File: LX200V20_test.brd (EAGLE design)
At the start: 74.9 x 45.7 mm, 32 parts

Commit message: Updated layout.
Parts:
- added STANDOFF5: STAND-OFF, SparkFun-Electromechanical:STAND-OFF
- added U$9: VREG-OKI-78SR, BlueRobotics-Main:OKI-78SR
- moved LED3 54.3 mm to (3.17, 32.4), turned to 270 degrees
- moved R7 54.3 mm to (3.17, 35.6), turned to 180 degrees
- moved LED4 53.5 mm to (3.17, 25.4), turned to 270 degrees
- moved R8 53.5 mm to (3.17, 28.6), turned to 180 degrees
- moved U$1 46.7 mm to (8.89, 3.81), turned to 90 degrees
- moved LED2 46.2 mm to (3.17, 17.8), turned to 270 degrees
- moved R6 46.2 mm to (3.17, 21.0), turned to 180 degrees
- moved LED1 42.2 mm to (3.17, 10.2), turned to 270 degrees
- moved R5 42.2 mm to (3.17, 13.3), turned to 180 degrees
- moved U$2 39.2 mm to (38.1, 18.4), turned to 0 degrees
- moved C4 34.4 mm to (20.3, 7.62), turned to 180 degrees
- moved U$3 29.6 mm to (16.5, 13.3), turned to 0 degrees
- moved C6 22.2 mm to (17.1, 19.7), turned to 180 degrees
- moved U$4 21.5 mm to (14.6, 38.1), turned to 270 degrees
- moved C1 21.0 mm to (17.1, 41.3), turned to 180 degrees
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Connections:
- removed net LED2: U$1.12
- net LED-ACT: now also U$1.12

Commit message: Removed AC components for DC-only support.
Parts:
- removed C5: 0.01uF 250V, resistor:C0805
- removed R9: 4.7K 1/4W, resistor:R1206
- C6: value 0.01uF 250V -> 0.01uF 500V; device resistor:C0805 -> resistor:C1206
- R10: value 4.7K 1/4W -> 10 1/4W
- moved C4 6.99 mm to (20.3, 14.6)
- moved U$3 5.12 mm to (14.0, 8.89)
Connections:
- removed net AC_CPLD_N: R9.2, U$3.6, U$5.2
- removed net N$12: C5.1, R9.1
- net EXT_AC_A: no longer C5.2
- net GND: now also U$3.6, U$5.2
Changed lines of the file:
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@@
 <element name="C2" library="resistor" package="C0402" value="0.1uF" x="17.145" y="26.035"/>
 <element name="C3" library="resistor" package="C1206" value="EFI Capacitor (1000 pF, 2kV)" x="29.845" y="33.655"/>
-<element name="C4" library="resistor" package="C0805" value="330pF 50V" x="20.32" y="7.62" rot="R180"/>
-<element name="C5" library="resistor" package="C0805" value="0.01uF 250V" x="17.145" y="22.225" rot="R180"/>
-<element name="C6" library="resistor" package="C0805" value="0.01uF 250V" x="17.145" y="19.685" rot="R180"/>
+<element name="C4" library="resistor" package="C0805" value="330pF 50V" x="20.32" y="14.605" rot="R180"/>
+<element name="C6" library="resistor" package="C1206" value="0.01uF 500V" x="17.145" y="19.685" rot="R180"/>
 <element name="LED1" library="led" package="CHIPLED_0603" value="" x="3.175" y="10.16" rot="R270"/>
 <element name="LED2" library="led" package="CHIPLED_0603" value="" x="3.175" y="17.78" rot="R270"/>
@@
 <element name="LED4" library="led" package="CHIPLED_0603" value="" x="3.175" y="25.4" rot="R270"/>
 <element name="R1" library="resistor" package="R0603" value="75" x="26.67" y="30.48" rot="R180"/>
-<element name="R10" library="resistor" package="R1206" value="4.7K 1/4W" x="22.225" y="19.685"/>
+<element name="R10" library="resistor" package="R1206" value="10 1/4W" x="22.225" y="19.685"/>
 <element name="R2" library="resistor" package="R0603" value="75" x="26.67" y="36.83" rot="R180"/>
 <element name="R3" library="resistor" package="R0603" value="75" x="30.48" y="36.83"/>
@@
 <element name="R7" library="resistor" package="R0603" value="470" x="3.175" y="35.56" rot="R180"/>
 <element name="R8" library="resistor" package="R0603" value="130" x="3.175" y="28.575" rot="R180"/>
-<element name="R9" library="resistor" package="R1206" value="4.7K 1/4W" x="22.225" y="22.225"/>
 <element name="U$1" library="BR-Eagle-Library" package="LX200V20" value="LX200V20" x="8.89" y="3.81" rot="R90"/>
 <element name="U$2" library="SparkFun-Connectors" package="RJ45-8" value="RJ45-8PTH" x="38.1" y="18.415"/>
-<element name="U$3" library="BlueRobotics-Main" package="PLC10005345" value="PLC10005345" x="16.51" y="13.335"/>
+<element name="U$3" library="BlueRobotics-Main" package="PLC10005345" value="PLC10005345" x="13.97" y="8.89"/>
 <element name="U$4" library="BlueRobotics-Main" package="PT61017PL" value="PT61017PEL" x="14.605" y="38.1" rot="R270"/>
 <element name="U$5" library="BlueRobotics-Main" package="SOD323-BIDIRECTIONAL" value="TVS-SP4021" x="26.035" y="20.955" rot="R90"/>
@@
 <contactref element="LED3" pad="C"/>
 <contactref element="LED4" pad="C"/>
-<wire x1="17.795" y1="26.035" x2="31.245" y2="33.655" width="0" layer="19" extent="1-1"/>
+<contactref element="U$5" pad="2"/>
+<contactref element="U$3" pad="6"/>
+<wire x1="26.035" y1="22.055" x2="31.245" y2="33.655" width="0" layer="19" extent="1-1"/>
+<wire x1="17.795" y1="26.035" x2="26.035" y2="22.055" width="0" layer="19" extent="1-1"/>
 <wire x1="7.49" y1="23.81" x2="17.795" y2="26.035" width="0" layer="19" extent="1-1"/>
 <wire x1="3.925" y1="25.4" x2="7.49" y2="23.81" width="0" layer="19" extent="1-1"/>
@@
 <wire x1="7.49" y1="3.81" x2="10.29" y2="9.81" width="0" layer="19" extent="1-1"/>
 <wire x1="16.495" y1="41.275" x2="7.49" y2="35.81" width="0" layer="19" extent="1-1"/>
+<wire x1="24.13" y1="6.35" x2="10.29" y2="9.81" width="0" layer="19" extent="1-1"/>
 </signal>
 <signal name="N$1">
@@
 <contactref element="U$3" pad="2"/>
 <contactref element="C4" pad="1"/>
-<wire x1="21.27" y1="7.62" x2="19.05" y2="10.795" width="0" layer="19" extent="1-1"/>
-<wire x1="10.29" y1="5.81" x2="19.05" y2="10.795" width="0" layer="19" extent="1-1"/>
+<wire x1="16.51" y1="6.35" x2="21.27" y2="14.605" width="0" layer="19" extent="1-1"/>
+<wire x1="10.29" y1="5.81" x2="16.51" y2="6.35" width="0" layer="19" extent="1-1"/>
 </signal>
 <signal name="TX-">
@@
 <contactref element="U$3" pad="1"/>
 <contactref element="C4" pad="2"/>
-<wire x1="19.37" y1="7.62" x2="19.05" y2="15.875" width="0" layer="19" extent="1-1"/>
-<wire x1="7.49" y1="7.81" x2="19.37" y2="7.62" width="0" layer="19" extent="1-1"/>
+<wire x1="16.51" y1="11.43" x2="19.37" y2="14.605" width="0" layer="19" extent="1-1"/>
+<wire x1="7.49" y1="7.81" x2="16.51" y2="11.43" width="0" layer="19" extent="1-1"/>
 </signal>
 <signal name="RX+">
 <contactref element="U$1" pad="5"/>
 <contactref element="U$3" pad="3"/>
-<wire x1="7.49" y1="11.81" x2="16.51" y2="15.875" width="0" layer="19" extent="1-1"/>
+<wire x1="7.49" y1="11.81" x2="13.97" y2="11.43" width="0" layer="19" extent="1-1"/>
 </signal>
 <signal name="RX-">
 <contactref element="U$1" pad="6"/>
 <contactref element="U$3" pad="4"/>
-<wire x1="10.29" y1="13.81" x2="16.51" y2="10.795" width="0" layer="19" extent="1-1"/>
+<wire x1="13.97" y1="6.35" x2="10.29" y2="13.81" width="0" layer="19" extent="1-1"/>
 </signal>
 <signal name="ZC_IN_EX">
 <contactref element="U$1" pad="8"/>
-</signal>
-<signal name="AC_CPLD_N">
-<contactref element="U$3" pad="6"/>
-<contactref element="R9" pad="2"/>
-<contactref element="U$5" pad="2"/>
-<wire x1="23.647" y1="22.225" x2="26.035" y2="22.055" width="0" layer="19" extent="1-1"/>
-<wire x1="26.67" y1="10.795" x2="26.035" y2="22.055" width="0" layer="19" extent="1-1"/>
 </signal>
 <signal name="N$6">
@@
 <contactref element="R10" pad="1"/>
 <contactref element="C6" pad="1"/>
-<wire x1="18.095" y1="19.685" x2="20.803" y2="19.685" width="0" layer="19" extent="1-1"/>
-</signal>
-<signal name="N$12">
-<contactref element="R9" pad="1"/>
-<contactref element="C5" pad="1"/>
-<wire x1="18.095" y1="22.225" x2="20.803" y2="22.225" width="0" layer="19" extent="1-1"/>
+<wire x1="18.545" y1="19.685" x2="20.803" y2="19.685" width="0" layer="19" extent="1-1"/>
 </signal>
 <signal name="EXT_AC_A">
-<contactref element="C5" pad="2"/>
 <contactref element="JP1" pad="3"/>
-<wire x1="16.195" y1="22.225" x2="36.845" y2="6.35" width="0" layer="19" extent="1-1"/>
 </signal>
 <signal name="EXT_AC_B">
 <contactref element="C6" pad="2"/>
 <contactref element="JP1" pad="4"/>
-<wire x1="16.195" y1="19.685" x2="40.345" y2="6.35" width="0" layer="19" extent="1-1"/>
+<wire x1="15.745" y1="19.685" x2="40.345" y2="6.35" width="0" layer="19" extent="1-1"/>
 </signal>
 <signal name="AC_CPLD_L">
@@
 <contactref element="U$5" pad="1"/>
 <wire x1="23.647" y1="19.685" x2="26.035" y2="19.855" width="0" layer="19" extent="1-1"/>
-<wire x1="26.67" y1="15.875" x2="26.035" y2="19.855" width="0" layer="19" extent="1-1"/>
+<wire x1="24.13" y1="11.43" x2="23.647" y2="19.685" width="0" layer="19" extent="1-1"/>
 </signal>
 </signals>

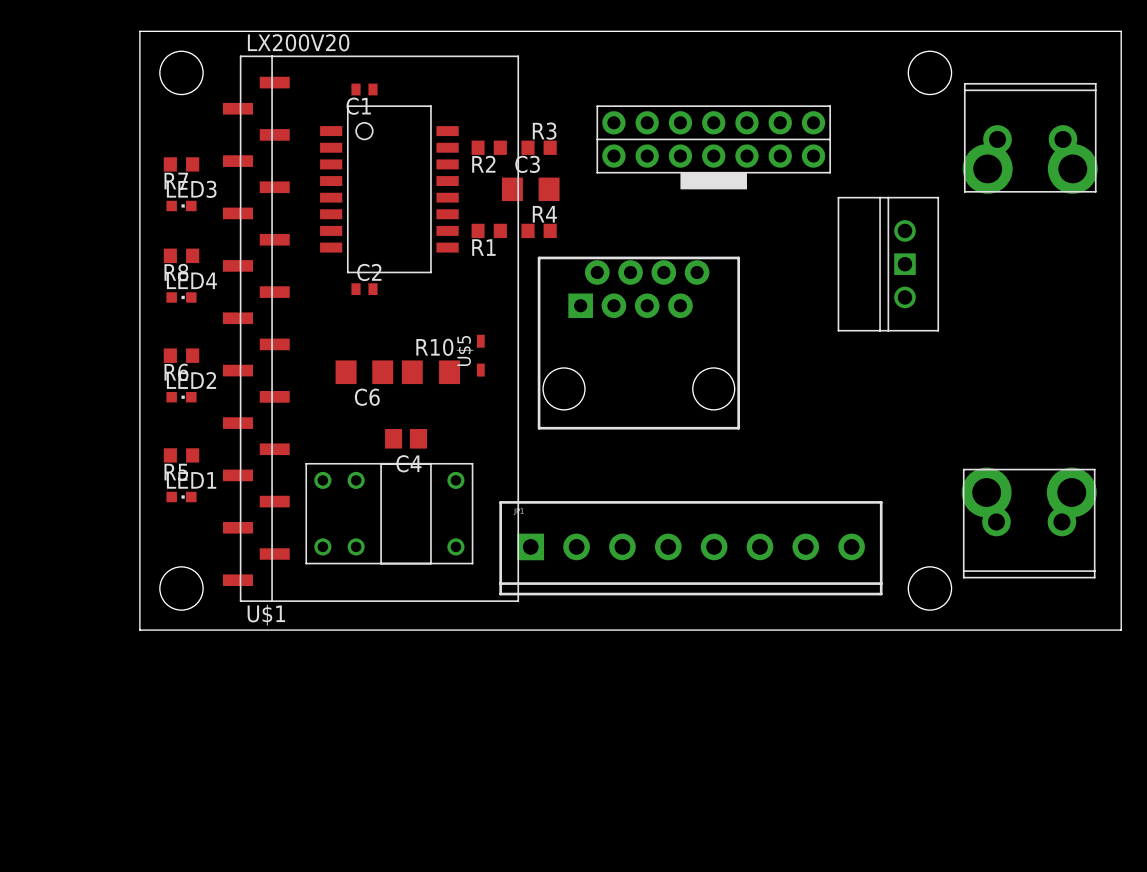
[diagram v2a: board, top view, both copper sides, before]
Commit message: Changing to Ethernet+Power only design.
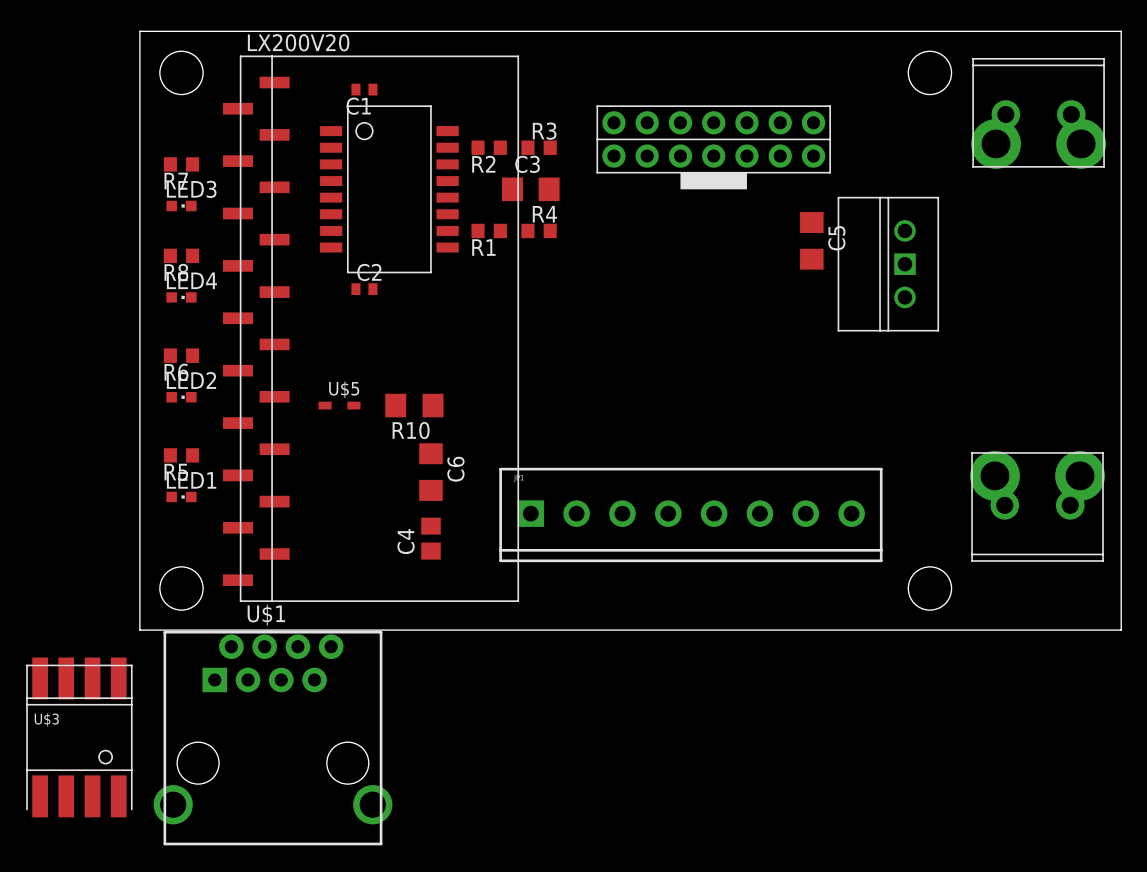
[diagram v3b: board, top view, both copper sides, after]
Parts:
- added C5: 10uF, resistor:C1206
- R10: value 10 1/4W -> 10 1/4W HV
- U$2: device SparkFun-Connectors:RJ45-8 -> BlueRobotics-Main:RJ45-8-VERT
- U$3: value PLC10005345 -> UT11403S; device BlueRobotics-Main:PLC10005345 -> BlueRobotics-Main:UT11403S
- U$9: value VREG-OKI-78SR -> OKI-78SR-3.3V
- moved U$2 40.0 mm to (10.2, -10.2)
- moved U$7 31.6 mm to (71.1, 39.4), turned to 180 degrees
- moved U$3 30.5 mm to (-7.62, -12.7)
- moved U$8 28.3 mm to (66.0, 9.53), turned to 0 degrees
- moved U$5 11.4 mm to (15.2, 17.1), turned to 0 degrees
- moved C6 9.16 mm to (22.2, 12.1), turned to 270 degrees
- moved C4 7.85 mm to (22.2, 6.99), turned to 90 degrees
- moved R10 2.84 mm to (21.0, 17.1), turned to 180 degrees
- moved JP1 2.54 mm to (29.8, 8.89)
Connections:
- net EXT_AC_B renamed HV_SIGNAL
- removed net AC_CPLD_L: R10.2, U$3.5, U$5.1
- removed net EXT_AC_A: JP1.3
- new net 3.3V: C5.1, U$9.OUTPUT
- new net GNDI: JP1.3, U$3.PL_L, U$5.2
- new net PL_N: R10.2, U$3.PL_N, U$5.1
- new net VIN: U$7.2A, U$7.2B, U$9.INPUT
- net GND: now also C5.2, U$7.1A, U$7.1B, U$9.GND; no longer U$3.6, U$5.2
- net RX+: now also U$3.RX+; no longer U$3.3
- net RX-: now also U$3.RX-; no longer U$3.4
- net TX+: now also U$3.TX+; no longer U$3.2
- net TX-: now also U$3.TX-; no longer U$3.1
